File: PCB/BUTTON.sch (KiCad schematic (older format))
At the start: 4 parts, among them J6 BUTTON, SW2 BUTTON

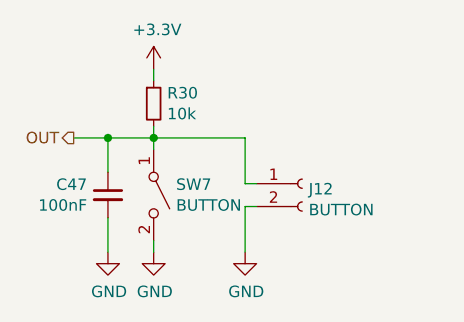
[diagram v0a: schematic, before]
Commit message: Added some footprints
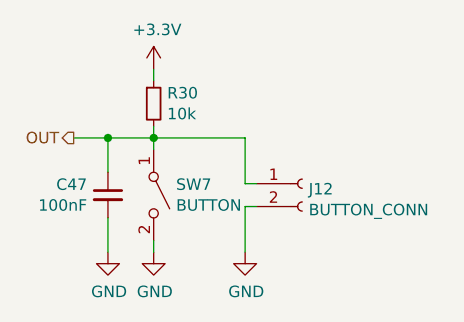
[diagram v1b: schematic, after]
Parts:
- J6: value BUTTON -> BUTTON_CONN
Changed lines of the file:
@@
 $Descr A4 11693 8268
 encoding utf-8
-Sheet 8 20
+Sheet 20 20
 Title ""
 Date ""
@@
 AR Path="/5E8CBE93/5E87809C" Ref="#PWR0136"  Part="1"
 AR Path="/5E8CBE97/5E87809C" Ref="#PWR0140"  Part="1"
-F 0 "#PWR061" H 5650 3450 50  0001 C CNN
+F 0 "#PWR0140" H 5650 3450 50  0001 C CNN
 F 1 "+3.3V" H 5665 3773 50  0000 C CNN
 F 2 "" H 5650 3600 50  0001 C CNN
@@
 AR Path="/5E8CBE93/5E87834C" Ref="#PWR0137"  Part="1"
 AR Path="/5E8CBE97/5E87834C" Ref="#PWR0141"  Part="1"
-F 0 "#PWR062" H 5650 4150 50  0001 C CNN
+F 0 "#PWR0141" H 5650 4150 50  0001 C CNN
 F 1 "GND" H 5655 4227 50  0000 C CNN
 F 2 "" H 5650 4400 50  0001 C CNN
@@
 AR Path="/5E8CBE97/5E879014" Ref="J12"  Part="1"
 F 0 "J12" H 6328 4076 50  0000 L CNN
-F 1 "BUTTON" H 6328 3985 50  0000 L CNN
+F 1 "BUTTON_CONN" H 6328 3985 50  0000 L CNN
 F 2 "" H 6300 4100 50  0001 C CNN
 F 3 "" H 6300 4100 50  0001 C CNN
@@
 AR Path="/5E8CBE93/5E879541" Ref="#PWR0138"  Part="1"
 AR Path="/5E8CBE97/5E879541" Ref="#PWR0142"  Part="1"
-F 0 "#PWR063" H 6050 4150 50  0001 C CNN
+F 0 "#PWR0142" H 6050 4150 50  0001 C CNN
 F 1 "GND" H 6055 4227 50  0000 C CNN
 F 2 "" H 6050 4400 50  0001 C CNN
@@
 AR Path="/5E8CBE93/5E87C4B2" Ref="#PWR0135"  Part="1"
 AR Path="/5E8CBE97/5E87C4B2" Ref="#PWR0139"  Part="1"
-F 0 "#PWR060" H 5450 4150 50  0001 C CNN
+F 0 "#PWR0139" H 5450 4150 50  0001 C CNN
 F 1 "GND" H 5455 4227 50  0000 C CNN
 F 2 "" H 5450 4400 50  0001 C CNN

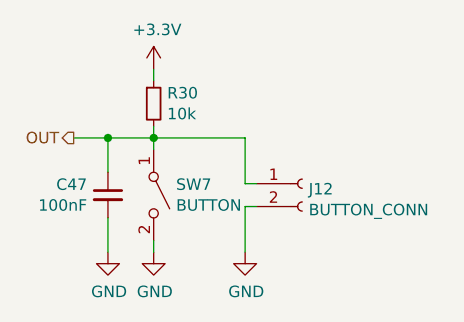
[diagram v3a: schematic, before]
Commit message: Increased VCC from 3v3 to 5v
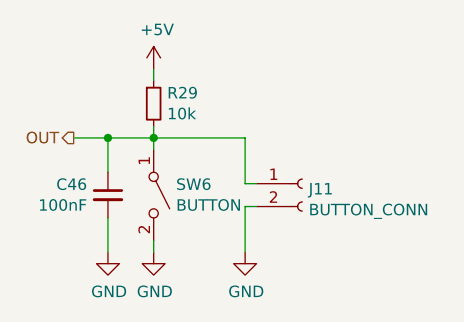
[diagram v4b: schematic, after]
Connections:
- net +3V3 renamed +5V
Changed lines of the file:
@@
 AR Path="/5E8CBE93/5E8777C3" Ref="SW6"  Part="1"
 AR Path="/5E8CBE97/5E8777C3" Ref="SW7"  Part="1"
-F 0 "SW7" V 5604 4248 50  0000 L CNN
+F 0 "SW6" V 5604 4248 50  0000 L CNN
 F 1 "BUTTON" V 5695 4248 50  0000 L CNN
 F 2 "" H 5650 4150 50  0001 C CNN
@@
 AR Path="/5E8CBE93/5E877C7D" Ref="R29"  Part="1"
 AR Path="/5E8CBE97/5E877C7D" Ref="R30"  Part="1"
-F 0 "R30" H 5709 3796 50  0000 L CNN
+F 0 "R29" H 5709 3796 50  0000 L CNN
 F 1 "10k" H 5709 3705 50  0000 L CNN
 F 2 "" H 5650 3750 50  0001 C CNN
@@
 Wire Wire Line
 	5650 3850 5650 3900
-$Comp
-L power:+3.3V #PWR061
-U 1 1 5E87809C
-P 5650 3600
-AR Path="/5E8776DF/5E87809C" Ref="#PWR061"  Part="1"
-AR Path="/5E8CBD7F/5E87809C" Ref="#PWR0132"  Part="1"
-AR Path="/5E8CBE93/5E87809C" Ref="#PWR0136"  Part="1"
-AR Path="/5E8CBE97/5E87809C" Ref="#PWR0140"  Part="1"
-F 0 "#PWR0140" H 5650 3450 50  0001 C CNN
-F 1 "+3.3V" H 5665 3773 50  0000 C CNN
-F 2 "" H 5650 3600 50  0001 C CNN
-F 3 "" H 5650 3600 50  0001 C CNN
-	1    5650 3600
-	1    0    0    -1
-$EndComp
 Wire Wire Line
 	5650 3600 5650 3650
@@
 AR Path="/5E8CBE93/5E87834C" Ref="#PWR0137"  Part="1"
 AR Path="/5E8CBE97/5E87834C" Ref="#PWR0141"  Part="1"
-F 0 "#PWR0141" H 5650 4150 50  0001 C CNN
+F 0 "#PWR0137" H 5650 4150 50  0001 C CNN
 F 1 "GND" H 5655 4227 50  0000 C CNN
 F 2 "" H 5650 4400 50  0001 C CNN
@@
 AR Path="/5E8CBE93/5E879014" Ref="J11"  Part="1"
 AR Path="/5E8CBE97/5E879014" Ref="J12"  Part="1"
-F 0 "J12" H 6328 4076 50  0000 L CNN
+F 0 "J11" H 6328 4076 50  0000 L CNN
 F 1 "BUTTON_CONN" H 6328 3985 50  0000 L CNN
 F 2 "" H 6300 4100 50  0001 C CNN
@@
 AR Path="/5E8CBE93/5E879541" Ref="#PWR0138"  Part="1"
 AR Path="/5E8CBE97/5E879541" Ref="#PWR0142"  Part="1"
-F 0 "#PWR0142" H 6050 4150 50  0001 C CNN
+F 0 "#PWR0138" H 6050 4150 50  0001 C CNN
 F 1 "GND" H 6055 4227 50  0000 C CNN
 F 2 "" H 6050 4400 50  0001 C CNN
@@
 AR Path="/5E8CBE93/5E87BCDD" Ref="C46"  Part="1"
 AR Path="/5E8CBE97/5E87BCDD" Ref="C47"  Part="1"
-F 0 "C47" H 5359 4196 50  0000 R CNN
+F 0 "C46" H 5359 4196 50  0000 R CNN
 F 1 "100nF" H 5359 4105 50  0000 R CNN
 F 2 "" H 5450 4150 50  0001 C CNN
@@
 AR Path="/5E8CBE93/5E87C4B2" Ref="#PWR0135"  Part="1"
 AR Path="/5E8CBE97/5E87C4B2" Ref="#PWR0139"  Part="1"
-F 0 "#PWR0139" H 5450 4150 50  0001 C CNN
+F 0 "#PWR0135" H 5450 4150 50  0001 C CNN
 F 1 "GND" H 5455 4227 50  0000 C CNN
 F 2 "" H 5450 4400 50  0001 C CNN
@@
 Wire Wire Line
 	5450 4400 5450 4250
+$Comp
+L power:+5V #PWR?
+U 1 1 5E91F8C0
+P 5650 3600
+AR Path="/5E8A6686/5E91F8C0" Ref="#PWR?"  Part="1"
+AR Path="/5E8776DF/5E91F8C0" Ref="#PWR?"  Part="1"
+AR Path="/5E8CBE97/5E91F8C0" Ref="#PWR?"  Part="1"
+AR Path="/5E8CBE93/5E91F8C0" Ref="#PWR?"  Part="1"
+F 0 "#PWR?" H 5650 3450 50  0001 C CNN
+F 1 "+5V" H 5665 3773 50  0000 C CNN
+F 2 "" H 5650 3600 50  0001 C CNN
+F 3 "" H 5650 3600 50  0001 C CNN
+	1    5650 3600
+	1    0    0    -1
+$EndComp
 $EndSCHEMATC

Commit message: Added Humidity and temperature sensors
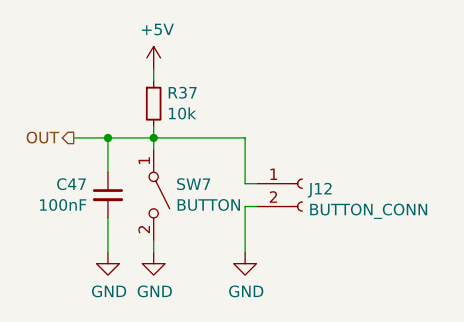
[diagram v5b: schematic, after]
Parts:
- renumbered R9 to R14
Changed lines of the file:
@@
 AR Path="/5E8CBE93/5E8777C3" Ref="SW6"  Part="1"
 AR Path="/5E8CBE97/5E8777C3" Ref="SW7"  Part="1"
-F 0 "SW6" V 5604 4248 50  0000 L CNN
+F 0 "SW7" V 5604 4248 50  0000 L CNN
 F 1 "BUTTON" V 5695 4248 50  0000 L CNN
 F 2 "" H 5650 4150 50  0001 C CNN
@@
 $EndComp
 $Comp
-L Device:R_Small R9
+L Device:R_Small R14
 U 1 1 5E877C7D
 P 5650 3750
-AR Path="/5E8776DF/5E877C7D" Ref="R9"  Part="1"
-AR Path="/5E8CBD7F/5E877C7D" Ref="R28"  Part="1"
-AR Path="/5E8CBE93/5E877C7D" Ref="R29"  Part="1"
-AR Path="/5E8CBE97/5E877C7D" Ref="R30"  Part="1"
-F 0 "R29" H 5709 3796 50  0000 L CNN
+AR Path="/5E8776DF/5E877C7D" Ref="R14"  Part="1"
+AR Path="/5E8CBD7F/5E877C7D" Ref="R35"  Part="1"
+AR Path="/5E8CBE93/5E877C7D" Ref="R36"  Part="1"
+AR Path="/5E8CBE97/5E877C7D" Ref="R37"  Part="1"
+F 0 "R37" H 5709 3796 50  0000 L CNN
 F 1 "10k" H 5709 3705 50  0000 L CNN
 F 2 "" H 5650 3750 50  0001 C CNN
@@
 	5650 3600 5650 3650
 $Comp
-L power:GND #PWR062
+L power:GND #PWR064
 U 1 1 5E87834C
 P 5650 4400
-AR Path="/5E8776DF/5E87834C" Ref="#PWR062"  Part="1"
-AR Path="/5E8CBD7F/5E87834C" Ref="#PWR0133"  Part="1"
-AR Path="/5E8CBE93/5E87834C" Ref="#PWR0137"  Part="1"
-AR Path="/5E8CBE97/5E87834C" Ref="#PWR0141"  Part="1"
-F 0 "#PWR0137" H 5650 4150 50  0001 C CNN
+AR Path="/5E8776DF/5E87834C" Ref="#PWR064"  Part="1"
+AR Path="/5E8CBD7F/5E87834C" Ref="#PWR0136"  Part="1"
+AR Path="/5E8CBE93/5E87834C" Ref="#PWR0140"  Part="1"
+AR Path="/5E8CBE97/5E87834C" Ref="#PWR0144"  Part="1"
+F 0 "#PWR0144" H 5650 4150 50  0001 C CNN
 F 1 "GND" H 5655 4227 50  0000 C CNN
 F 2 "" H 5650 4400 50  0001 C CNN
@@
 AR Path="/5E8CBE93/5E879014" Ref="J11"  Part="1"
 AR Path="/5E8CBE97/5E879014" Ref="J12"  Part="1"
-F 0 "J11" H 6328 4076 50  0000 L CNN
+F 0 "J12" H 6328 4076 50  0000 L CNN
 F 1 "BUTTON_CONN" H 6328 3985 50  0000 L CNN
 F 2 "" H 6300 4100 50  0001 C CNN
@@
 	6050 3900 5650 3900
 $Comp
-L power:GND #PWR063
+L power:GND #PWR065
 U 1 1 5E879541
 P 6050 4400
-AR Path="/5E8776DF/5E879541" Ref="#PWR063"  Part="1"
-AR Path="/5E8CBD7F/5E879541" Ref="#PWR0134"  Part="1"
-AR Path="/5E8CBE93/5E879541" Ref="#PWR0138"  Part="1"
-AR Path="/5E8CBE97/5E879541" Ref="#PWR0142"  Part="1"
-F 0 "#PWR0138" H 6050 4150 50  0001 C CNN
+AR Path="/5E8776DF/5E879541" Ref="#PWR065"  Part="1"
+AR Path="/5E8CBD7F/5E879541" Ref="#PWR0137"  Part="1"
+AR Path="/5E8CBE93/5E879541" Ref="#PWR0141"  Part="1"
+AR Path="/5E8CBE97/5E879541" Ref="#PWR0145"  Part="1"
+F 0 "#PWR0145" H 6050 4150 50  0001 C CNN
 F 1 "GND" H 6055 4227 50  0000 C CNN
 F 2 "" H 6050 4400 50  0001 C CNN
@@
 AR Path="/5E8CBE93/5E87BCDD" Ref="C46"  Part="1"
 AR Path="/5E8CBE97/5E87BCDD" Ref="C47"  Part="1"
-F 0 "C46" H 5359 4196 50  0000 R CNN
+F 0 "C47" H 5359 4196 50  0000 R CNN
 F 1 "100nF" H 5359 4105 50  0000 R CNN
 F 2 "" H 5450 4150 50  0001 C CNN
@@
 	5450 3900 5650 3900
 $Comp
-L power:GND #PWR060
+L power:GND #PWR062
 U 1 1 5E87C4B2
 P 5450 4400
-AR Path="/5E8776DF/5E87C4B2" Ref="#PWR060"  Part="1"
-AR Path="/5E8CBD7F/5E87C4B2" Ref="#PWR0131"  Part="1"
-AR Path="/5E8CBE93/5E87C4B2" Ref="#PWR0135"  Part="1"
-AR Path="/5E8CBE97/5E87C4B2" Ref="#PWR0139"  Part="1"
-F 0 "#PWR0135" H 5450 4150 50  0001 C CNN
+AR Path="/5E8776DF/5E87C4B2" Ref="#PWR062"  Part="1"
+AR Path="/5E8CBD7F/5E87C4B2" Ref="#PWR0134"  Part="1"
+AR Path="/5E8CBE93/5E87C4B2" Ref="#PWR0138"  Part="1"
+AR Path="/5E8CBE97/5E87C4B2" Ref="#PWR0142"  Part="1"
+F 0 "#PWR0142" H 5450 4150 50  0001 C CNN
 F 1 "GND" H 5455 4227 50  0000 C CNN
 F 2 "" H 5450 4400 50  0001 C CNN
@@
 P 5650 3600
 AR Path="/5E8A6686/5E91F8C0" Ref="#PWR?"  Part="1"
-AR Path="/5E8776DF/5E91F8C0" Ref="#PWR?"  Part="1"
-AR Path="/5E8CBE97/5E91F8C0" Ref="#PWR?"  Part="1"
-AR Path="/5E8CBE93/5E91F8C0" Ref="#PWR?"  Part="1"
-F 0 "#PWR?" H 5650 3450 50  0001 C CNN
+AR Path="/5E8776DF/5E91F8C0" Ref="#PWR063"  Part="1"
+AR Path="/5E8CBE97/5E91F8C0" Ref="#PWR0143"  Part="1"
+AR Path="/5E8CBE93/5E91F8C0" Ref="#PWR0139"  Part="1"
+AR Path="/5E8CBD7F/5E91F8C0" Ref="#PWR0135"  Part="1"
+F 0 "#PWR0143" H 5650 3450 50  0001 C CNN
 F 1 "+5V" H 5665 3773 50  0000 C CNN
 F 2 "" H 5650 3600 50  0001 C CNN

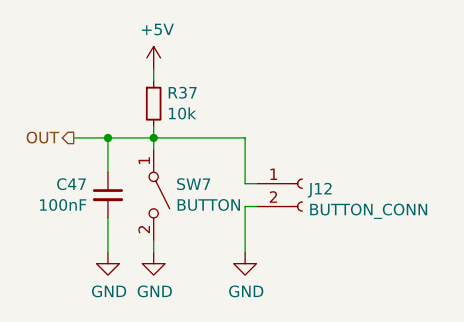
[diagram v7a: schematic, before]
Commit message: Added IEC connector and organised
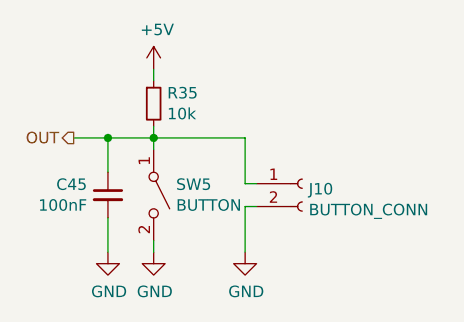
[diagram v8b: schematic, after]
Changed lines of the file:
@@
 AR Path="/5E8CBE93/5E8777C3" Ref="SW6"  Part="1"
 AR Path="/5E8CBE97/5E8777C3" Ref="SW7"  Part="1"
-F 0 "SW7" V 5604 4248 50  0000 L CNN
+F 0 "SW5" V 5604 4248 50  0000 L CNN
 F 1 "BUTTON" V 5695 4248 50  0000 L CNN
 F 2 "" H 5650 4150 50  0001 C CNN
@@
 AR Path="/5E8CBE93/5E877C7D" Ref="R36"  Part="1"
 AR Path="/5E8CBE97/5E877C7D" Ref="R37"  Part="1"
-F 0 "R37" H 5709 3796 50  0000 L CNN
+F 0 "R35" H 5709 3796 50  0000 L CNN
 F 1 "10k" H 5709 3705 50  0000 L CNN
 F 2 "" H 5650 3750 50  0001 C CNN
@@
 AR Path="/5E8CBE93/5E87834C" Ref="#PWR0140"  Part="1"
 AR Path="/5E8CBE97/5E87834C" Ref="#PWR0144"  Part="1"
-F 0 "#PWR0144" H 5650 4150 50  0001 C CNN
+F 0 "#PWR0136" H 5650 4150 50  0001 C CNN
 F 1 "GND" H 5655 4227 50  0000 C CNN
 F 2 "" H 5650 4400 50  0001 C CNN
@@
 AR Path="/5E8CBE93/5E879014" Ref="J11"  Part="1"
 AR Path="/5E8CBE97/5E879014" Ref="J12"  Part="1"
-F 0 "J12" H 6328 4076 50  0000 L CNN
+F 0 "J10" H 6328 4076 50  0000 L CNN
 F 1 "BUTTON_CONN" H 6328 3985 50  0000 L CNN
 F 2 "" H 6300 4100 50  0001 C CNN
@@
 AR Path="/5E8CBE93/5E879541" Ref="#PWR0141"  Part="1"
 AR Path="/5E8CBE97/5E879541" Ref="#PWR0145"  Part="1"
-F 0 "#PWR0145" H 6050 4150 50  0001 C CNN
+F 0 "#PWR0137" H 6050 4150 50  0001 C CNN
 F 1 "GND" H 6055 4227 50  0000 C CNN
 F 2 "" H 6050 4400 50  0001 C CNN
@@
 AR Path="/5E8CBE93/5E87BCDD" Ref="C46"  Part="1"
 AR Path="/5E8CBE97/5E87BCDD" Ref="C47"  Part="1"
-F 0 "C47" H 5359 4196 50  0000 R CNN
+F 0 "C45" H 5359 4196 50  0000 R CNN
 F 1 "100nF" H 5359 4105 50  0000 R CNN
 F 2 "" H 5450 4150 50  0001 C CNN
@@
 AR Path="/5E8CBE93/5E87C4B2" Ref="#PWR0138"  Part="1"
 AR Path="/5E8CBE97/5E87C4B2" Ref="#PWR0142"  Part="1"
-F 0 "#PWR0142" H 5450 4150 50  0001 C CNN
+F 0 "#PWR0134" H 5450 4150 50  0001 C CNN
 F 1 "GND" H 5455 4227 50  0000 C CNN
 F 2 "" H 5450 4400 50  0001 C CNN
@@
 AR Path="/5E8CBE93/5E91F8C0" Ref="#PWR0139"  Part="1"
 AR Path="/5E8CBD7F/5E91F8C0" Ref="#PWR0135"  Part="1"
-F 0 "#PWR0143" H 5650 3450 50  0001 C CNN
+F 0 "#PWR0135" H 5650 3450 50  0001 C CNN
 F 1 "+5V" H 5665 3773 50  0000 C CNN
 F 2 "" H 5650 3600 50  0001 C CNN
